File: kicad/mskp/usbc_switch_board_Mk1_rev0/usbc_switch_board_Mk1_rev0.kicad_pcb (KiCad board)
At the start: 2 copper layers, 23 parts, among them J1 USB_C_Receptacle_USB2.0_14P, J2 USB_C_Receptacle_USB2.0_14P, J3 USB_A, J4 USB_out_pads, J5 switch_ctrl_pads, Q1 2N3906, Q2 2N3904, U1 FSUSB42MUX, U2 AMS1117-3.3

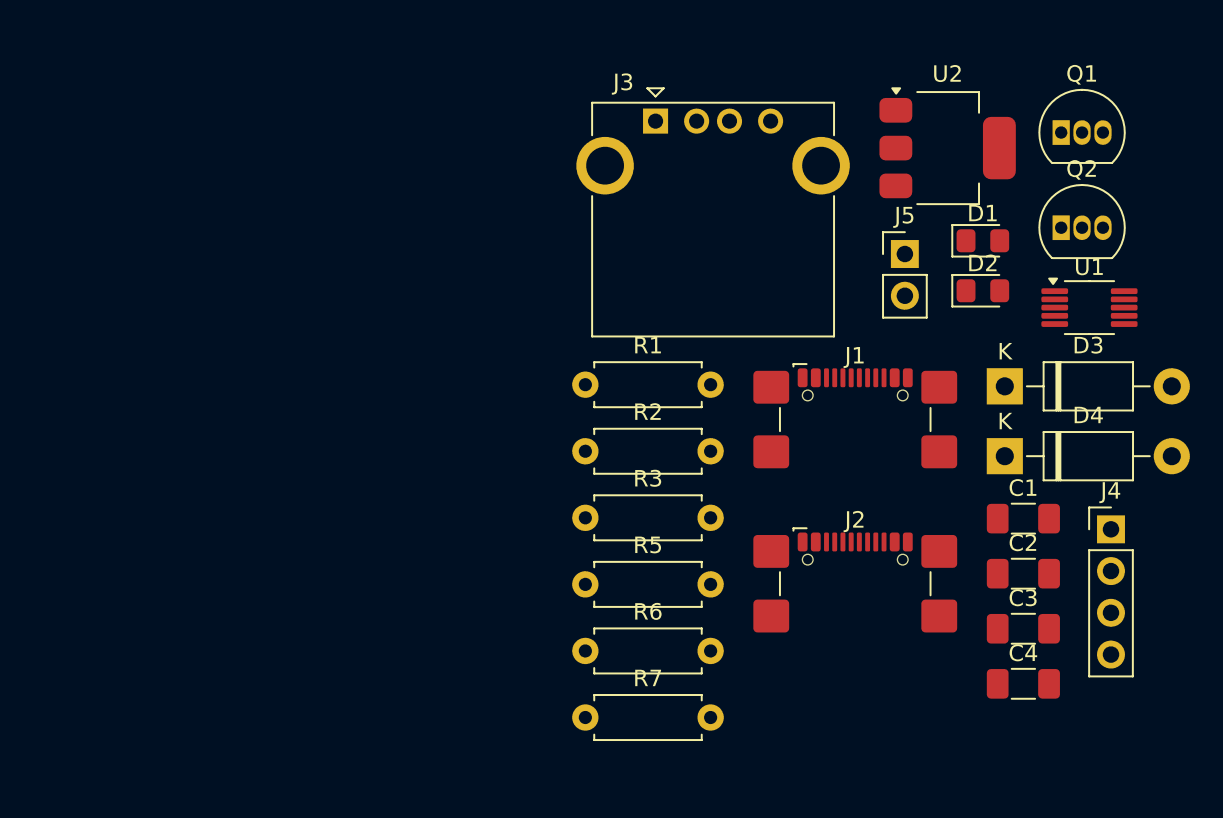
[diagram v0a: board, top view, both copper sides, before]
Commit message: Begins rough PCB part grouping for all control board revisions
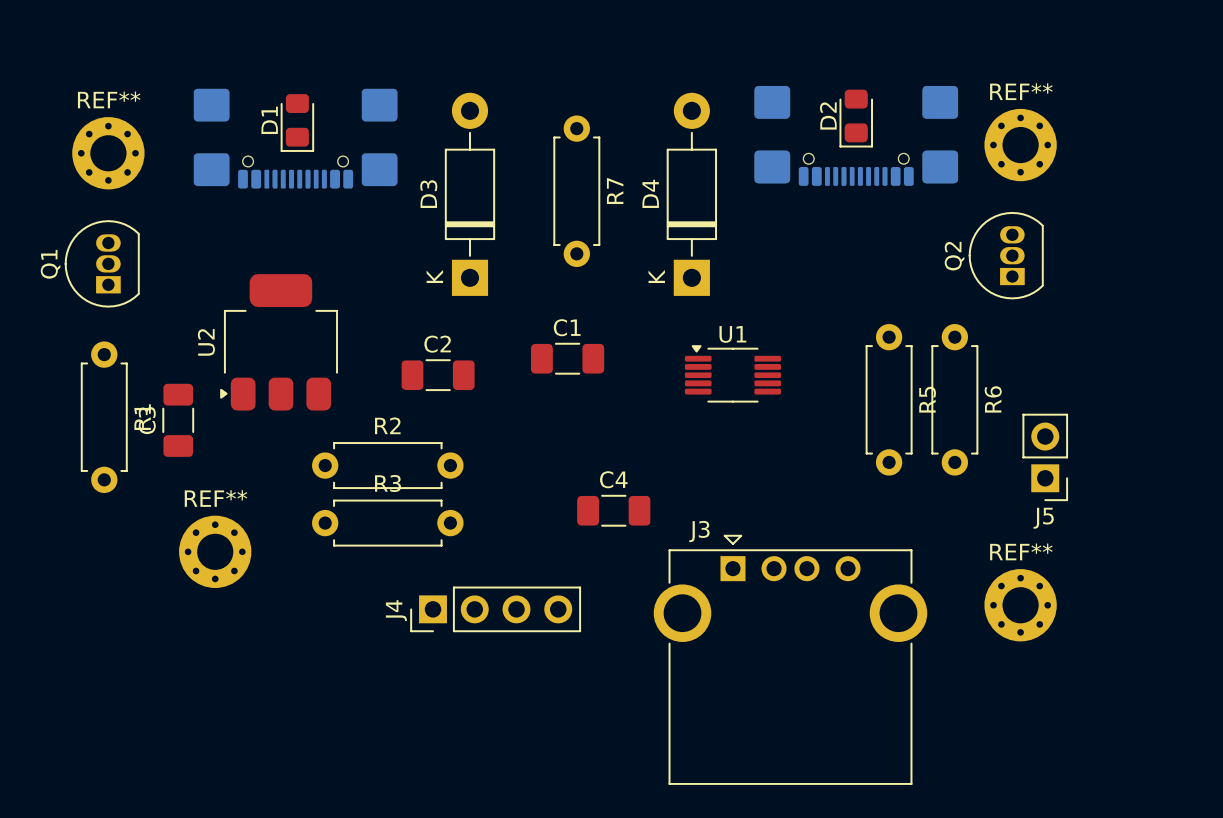
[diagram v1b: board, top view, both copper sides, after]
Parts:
- added REF**: MountingHole_2.2mm_M2_Pad_Via, MountingHole:MountingHole_2.2mm_M2_Pad_Via, F.Cu at (159.5, 97.0)
- added REF**: MountingHole_2.2mm_M2_Pad_Via, MountingHole:MountingHole_2.2mm_M2_Pad_Via, F.Cu at (159.5, 69.0)
- added REF**: MountingHole_2.2mm_M2_Pad_Via, MountingHole:MountingHole_2.2mm_M2_Pad_Via, F.Cu at (104.0, 69.5)
- added REF**: MountingHole_2.2mm_M2_Pad_Via, MountingHole:MountingHole_2.2mm_M2_Pad_Via, F.Cu at (110.5, 93.8)
- J1, J2: moved to B.Cu
- moved Q1 58.7 mm to (104.0, 77.5), turned to 90 degrees
- moved C3 53.0 mm to (108.2, 85.8), turned to 90 degrees
- moved D1 42.3 mm to (115.5, 67.5), turned to 90 degrees
- moved U2 42.2 mm to (114.5, 81.0), turned to 90 degrees
- moved J4 41.5 mm to (123.8, 97.2), turned to 90 degrees
- moved J1 39.2 mm to (115.4, 67.4)
- moved C2 37.6 mm to (124.1, 83.0)
- moved R7 35.8 mm to (132.5, 68.0), turned to -90 degrees
- moved D3 33.2 mm to (126.0, 77.1), turned to 90 degrees
- moved J2 29.6 mm to (149.5, 67.2)
- moved R6 29.5 mm to (155.5, 80.7), turned to -90 degrees
- moved C1 29.4 mm to (131.9, 82.0)
- moved R1 29.3 mm to (103.8, 81.8), turned to -90 degrees
- moved J3 27.6 mm to (142.0, 94.8)
- moved C4 27.1 mm to (134.8, 91.2)
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
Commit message: Continues work with rough PCB outlines
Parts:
- moved C3 14.3 mm to (122.5, 84.9), turned to 180 degrees
- moved J3 7.97 mm to (138.2, 87.7)
- moved R6 7.48 mm to (148.1, 79.8), turned to 0 degrees
- moved REF** 7.16 mm to (154.4, 91.9)
- moved J5 6.10 mm to (155.2, 87.4), turned to -90 degrees
- moved C4 5.94 mm to (129.5, 88.4)
- moved R2 5.94 mm to (111.3, 88.5)
- moved R3 5.94 mm to (111.3, 92.0)
- moved Q2 5.89 mm to (153.2, 76.3)
- moved REF** 5.07 mm to (154.4, 69.2)
- moved J2 4.94 mm to (144.8, 68.6)
- moved D2 4.87 mm to (144.8, 68.4), turned to 0 degrees
- moved J4 4.86 mm to (122.9, 92.5)
- moved REF** 4.80 mm to (106.0, 91.9)
- moved D4 4.48 mm to (135.2, 78.3)
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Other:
- board outline added: 54.4 x 29 mm

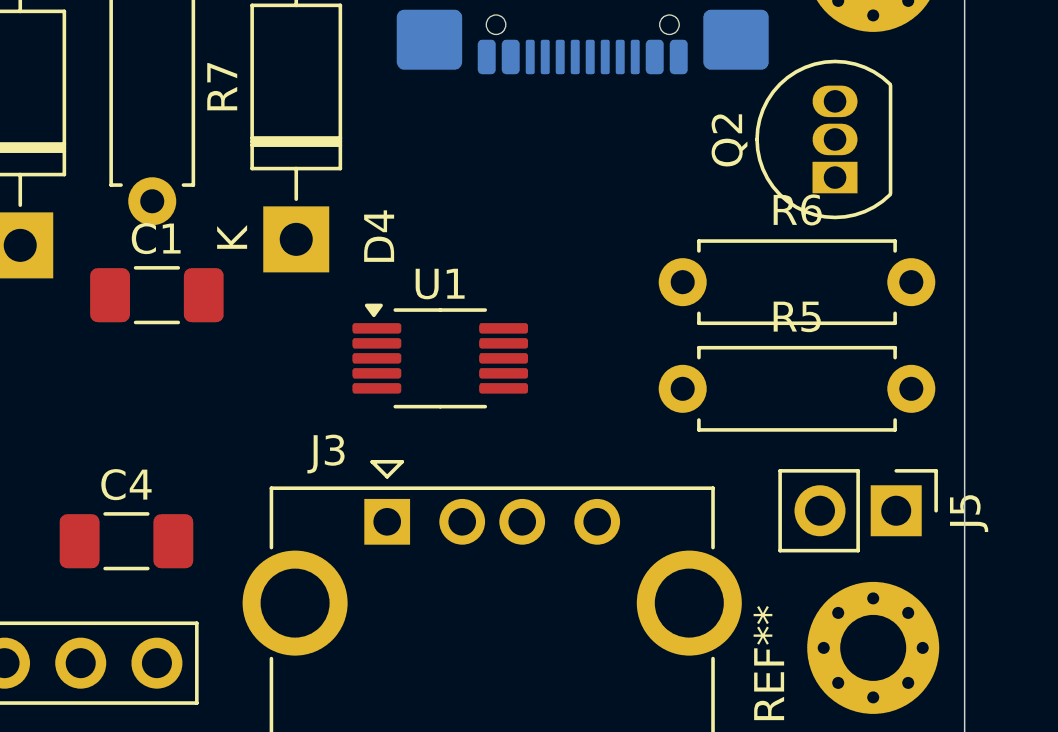
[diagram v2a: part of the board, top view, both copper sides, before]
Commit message: Refining PCB outlines for pico and io control boards
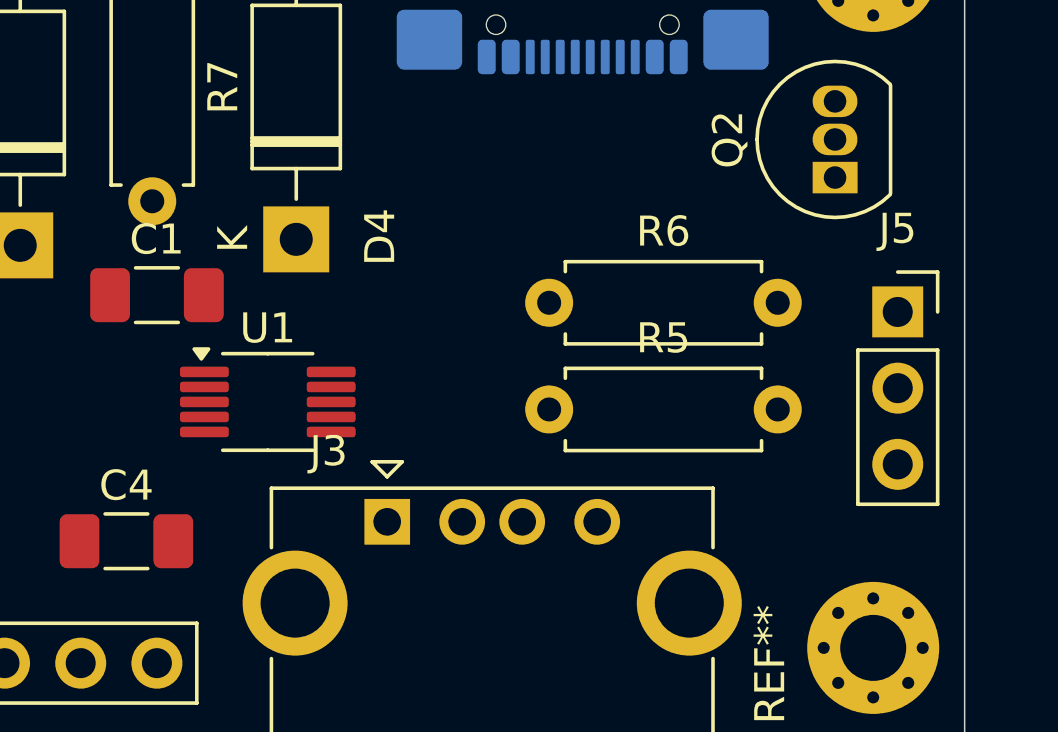
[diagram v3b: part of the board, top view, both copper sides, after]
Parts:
- J5: value switch_ctrl_pads -> Switch_ctrl_pads; footprint Connector_PinHeader_2.54mm:PinHeader_1x02_P2.54mm_Vertical -> Connector_PinSocket_2.54mm:PinSocket_1x03_P2.54mm_Vertical
- moved J5 6.63 mm to (155.2, 80.8), turned to 0 degrees
- moved U1 5.93 mm to (134.2, 83.8)
- moved R5 4.50 mm to (143.6, 84.0)
- moved R6 4.50 mm to (143.6, 80.4)
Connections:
- J5 pad 1: /SEL -> GND
- J5 pad 2: /SUS -> /SEL
- R6 pad 2: /SUS -> Net-(J5-Pin_3)
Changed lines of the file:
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@@
 	(net 16 "/D-")
 	(net 17 "/D+")
-	(net 18 "/SUS")
-	(net 19 "/SEL")
-	(net 20 "Net-(Q1-E)")
-	(net 21 "Net-(Q1-B)")
-	(net 22 "Net-(U2-GND)")
-	(net 23 "Net-(U1-SEL)")
-	(net 24 "Net-(U1-~{OE})")
+	(net 18 "/SEL")
+	(net 19 "Net-(Q1-E)")
+	(net 20 "Net-(Q1-B)")
+	(net 21 "Net-(U2-GND)")
+	(net 22 "Net-(U1-SEL)")
+	(net 23 "Net-(U1-~{OE})")
+	(net 24 "Net-(J5-Pin_3)")
 	(footprint "MountingHole:MountingHole_2.2mm_M2_Pad_Via"
 		(layer "F.Cu")
@@
 	(footprint "Package_SO:MSOP-10_3x3mm_P0.5mm"
 		(layer "F.Cu")
-		(at 140 82.296)
+		(at 134.25 83.75)
 		(descr "MSOP, 10 Pin (https://www.jedec.org/system/files/docs/mo-187F.pdf variant BA), generated with kicad-footprint-generator ipc_gullwing_generator.py")
 		(tags "MSOP SO")
@@
 			(layers "F.Cu" "F.Paste" "F.Mask")
 			(roundrect_rratio 0.25)
-			(net 23 "Net-(U1-SEL)")
+			(net 22 "Net-(U1-SEL)")
 			(pinfunction "SEL")
 			(pintype "input")
@@
 			(layers "F.Cu" "F.Paste" "F.Mask")
 			(roundrect_rratio 0.25)
-			(net 24 "Net-(U1-~{OE})")
+			(net 23 "Net-(U1-~{OE})")
 			(pinfunction "~{OE}")
 			(pintype "input")
@@
 			(layers "*.Cu" "*.Mask")
 			(remove_unused_layers no)
-			(net 20 "Net-(Q1-E)")
+			(net 19 "Net-(Q1-E)")
 			(pinfunction "E")
 			(pintype "passive")
@@
 			(layers "*.Cu" "*.Mask")
 			(remove_unused_layers no)
-			(net 21 "Net-(Q1-B)")
+			(net 20 "Net-(Q1-B)")
 			(pinfunction "B")
 			(pintype "input")
@@
 			(layers "*.Cu" "*.Mask")
 			(remove_unused_layers no)
-			(net 22 "Net-(U2-GND)")
+			(net 21 "Net-(U2-GND)")
 			(pintype "passive")
 		)
@@
 		(tags "LED handsolder")
 		(property "Reference" "D2"
-			(at 0 -1.65 360)
+			(at 0 -1.65 0)
 			(layer "F.SilkS")
 			(effects
@@
 		)
 		(property "Value" "LED"
-			(at 0 1.65 360)
+			(at 0 1.65 0)
 			(layer "F.Fab")
 			(effects
@@
 		)
 		(fp_text user "${REFERENCE}"
-			(at 0 0 360)
+			(at 0 0 0)
 			(layer "F.Fab")
 			(effects
@@
 	(footprint "Resistor_THT:R_Axial_DIN0207_L6.3mm_D2.5mm_P7.62mm_Horizontal"
 		(layer "F.Cu")
-		(at 148.082 79.756)
+		(at 143.63 80.444)
 		(descr "Resistor, Axial_DIN0207 series, Axial, Horizontal, pin pitch=7.62mm, 0.25W = 1/4W, length*diameter=6.3*2.5mm^2, http://cdn-reichelt.de/documents/datenblatt/B400/1_4W%23YAG.pdf")
 		(tags "Resistor Axial_DIN0207 series Axial Horizontal pin pitch 7.62mm 0.25W = 1/4W length 6.3mm diameter 2.5mm")
 		(property "Reference" "R6"
-			(at 3.81 -2.37 360)
+			(at 3.81 -2.37 0)
 			(layer "F.SilkS")
 			(effects
@@
 		)
 		(property "Value" "10K"
-			(at 3.81 2.37 360)
+			(at 3.81 2.37 0)
 			(layer "F.Fab")
 			(effects
@@
 		)
 		(fp_text user "${REFERENCE}"
-			(at 3.81 0 360)
+			(at 3.81 0 0)
 			(layer "F.Fab")
 			(effects
@@
 			(layers "*.Cu" "*.Mask")
 			(remove_unused_layers no)
-			(net 24 "Net-(U1-~{OE})")
+			(net 23 "Net-(U1-~{OE})")
 			(pintype "passive")
 		)
@@
 			(layers "*.Cu" "*.Mask")
 			(remove_unused_layers no)
-			(net 18 "/SUS")
+			(net 24 "Net-(J5-Pin_3)")
 			(pintype "passive")
 		)
@@
 			(layers "*.Cu" "*.Mask")
 			(remove_unused_layers no)
-			(net 21 "Net-(Q1-B)")
+			(net 20 "Net-(Q1-B)")
 			(pinfunction "B")
 			(pintype "passive")
@@
 			(layers "*.Cu" "*.Mask")
 			(remove_unused_layers no)
-			(net 20 "Net-(Q1-E)")
+			(net 19 "Net-(Q1-E)")
 			(pinfunction "C")
 			(pintype "passive")
@@
 			(layers "*.Cu" "*.Mask")
 			(remove_unused_layers no)
-			(net 20 "Net-(Q1-E)")
+			(net 19 "Net-(Q1-E)")
 			(pintype "passive")
 		)
@@
 			(layers "*.Cu" "*.Mask")
 			(remove_unused_layers no)
-			(net 21 "Net-(Q1-B)")
+			(net 20 "Net-(Q1-B)")
 			(pintype "passive")
 		)
@@
 			(layers "*.Cu" "*.Mask")
 			(remove_unused_layers no)
-			(net 19 "/SEL")
+			(net 18 "/SEL")
 			(pintype "passive")
 		)
@@
 		(tags "LED handsolder")
 		(property "Reference" "D1"
-			(at 0 -1.65 360)
+			(at 0 -1.65 0)
 			(layer "F.SilkS")
 			(effects
@@
 		)
 		(property "Value" "LED"
-			(at 0 1.65 360)
+			(at 0 1.65 0)
 			(layer "F.Fab")
 			(effects
@@
 		)
 		(fp_text user "${REFERENCE}"
-			(at 0 0 360)
+			(at 0 0 0)
 			(layer "F.Fab")
 			(effects
@@
 			(layers "*.Cu" "*.Mask")
 			(remove_unused_layers no)
-			(net 22 "Net-(U2-GND)")
+			(net 21 "Net-(U2-GND)")
 			(pintype "passive")
 		)
@@
 	(footprint "Resistor_THT:R_Axial_DIN0207_L6.3mm_D2.5mm_P7.62mm_Horizontal"
 		(layer "F.Cu")
-		(at 148.082 83.312)
+		(at 143.63 84)
 		(descr "Resistor, Axial_DIN0207 series, Axial, Horizontal, pin pitch=7.62mm, 0.25W = 1/4W, length*diameter=6.3*2.5mm^2, http://cdn-reichelt.de/documents/datenblatt/B400/1_4W%23YAG.pdf")
 		(tags "Resistor Axial_DIN0207 series Axial Horizontal pin pitch 7.62mm 0.25W = 1/4W length 6.3mm diameter 2.5mm")
 		(property "Reference" "R5"
-			(at 3.81 -2.37 360)
+			(at 3.81 -2.37 0)
 			(layer "F.SilkS")
 			(effects
@@
 		)
 		(property "Value" "10K"
-			(at 3.81 2.37 360)
+			(at 3.81 2.37 0)
 			(layer "F.Fab")
 			(effects
@@
 		)
 		(fp_text user "${REFERENCE}"
-			(at 3.81 0 360)
+			(at 3.81 0 0)
 			(layer "F.Fab")
 			(effects
@@
 			(layers "*.Cu" "*.Mask")
 			(remove_unused_layers no)
-			(net 23 "Net-(U1-SEL)")
+			(net 22 "Net-(U1-SEL)")
 			(pintype "passive")
 		)
@@
 			(layers "*.Cu" "*.Mask")
 			(remove_unused_layers no)
-			(net 19 "/SEL")
+			(net 18 "/SEL")
 			(pintype "passive")
 		)
@@
 		)
 	)
-	(footprint "Connector_PinHeader_2.54mm:PinHeader_1x02_P2.54mm_Vertical"
+	(footprint "Connector_PinSocket_2.54mm:PinSocket_1x03_P2.54mm_Vertical"
 		(layer "F.Cu")
-		(at 155.199 87.376 -90)
-		(descr "Through hole straight pin header, 1x02, 2.54mm pitch, single row")
-		(tags "Through hole pin header THT 1x02 2.54mm single row")
+		(at 155.25 80.75)
+		(descr "Through hole straight socket strip, 1x03, 2.54mm pitch, single row (from Kicad 4.0.7), script generated")
+		(tags "Through hole socket strip THT 1x03 2.54mm single row")
 		(property "Reference" "J5"
-			(at 0 -2.33 90)
+			(at 0 -2.77 0)
 			(layer "F.SilkS")
 			(effects
@@
 			)
 		)
-		(property "Value" "switch_ctrl_pads"
-			(at 0 4.87 90)
+		(property "Value" "Switch_ctrl_pads"
+			(at 0 7.85 0)
 			(layer "F.Fab")
 			(effects
@@
 			)
 		)
-		(property "Footprint" "Connector_PinHeader_2.54mm:PinHeader_1x02_P2.54mm_Vertical"
-			(at 0 0 -90)
+		(property "Footprint" "Connector_PinSocket_2.54mm:PinSocket_1x03_P2.54mm_Vertical"
+			(at 0 0 0)
 			(unlocked yes)
 			(layer "F.Fab")
@@
 		)
 		(property "Datasheet" ""
-			(at 0 0 -90)
+			(at 0 0 0)
 			(unlocked yes)
 			(layer "F.Fab")
@@
 			)
 		)
-		(property "Description" "Generic connector, single row, 01x02, script generated"
-			(at 0 0 -90)
+		(property "Description" "Generic connector, single row, 01x03, script generated"
+			(at 0 0 0)
 			(unlocked yes)
 			(layer "F.Fab")
@@
 		(attr through_hole)
 		(fp_line
-			(start -1.33 3.87)
-			(end 1.33 3.87)
+			(start -1.33 1.27)
+			(end -1.33 6.41)
 			(stroke
 				(width 0.12)
@@
 		(fp_line
 			(start -1.33 1.27)
-			(end -1.33 3.87)
+			(end 1.33 1.27)
 			(stroke
 				(width 0.12)
@@
 		)
 		(fp_line
-			(start -1.33 1.27)
-			(end 1.33 1.27)
+			(start -1.33 6.41)
+			(end 1.33 6.41)
 			(stroke
 				(width 0.12)
@@
 		)
 		(fp_line
-			(start 1.33 1.27)
-			(end 1.33 3.87)
+			(start 0 -1.33)
+			(end 1.33 -1.33)
 			(stroke
 				(width 0.12)
@@
 		)
 		(fp_line
-			(start -1.33 0)
-			(end -1.33 -1.33)
+			(start 1.33 -1.33)
+			(end 1.33 0)
 			(stroke
 				(width 0.12)
@@
 		)
 		(fp_line
-			(start -1.33 -1.33)
-			(end 0 -1.33)
+			(start 1.33 1.27)
+			(end 1.33 6.41)
 			(stroke
 				(width 0.12)
@@
 		)
 		(fp_line
-			(start -1.8 4.35)
-			(end 1.8 4.35)
+			(start -1.8 -1.8)
+			(end 1.75 -1.8)
 			(stroke
 				(width 0.05)
@@
 		)
 		(fp_line
-			(start 1.8 4.35)
-			(end 1.8 -1.8)
+			(start -1.8 6.85)
+			(end -1.8 -1.8)
 			(stroke
 				(width 0.05)
@@
 		)
 		(fp_line
-			(start -1.8 -1.8)
-			(end -1.8 4.35)
+			(start 1.75 -1.8)
+			(end 1.75 6.85)
 			(stroke
 				(width 0.05)
@@
 		)
 		(fp_line
-			(start 1.8 -1.8)
-			(end -1.8 -1.8)
+			(start 1.75 6.85)
+			(end -1.8 6.85)
 			(stroke
 				(width 0.05)
@@
 		)
 		(fp_line
-			(start -1.27 3.81)
-			(end -1.27 -0.635)
+			(start -1.27 -1.27)
+			(end 0.635 -1.27)
 			(stroke
 				(width 0.1)
@@
 		)
 		(fp_line
-			(start 1.27 3.81)
-			(end -1.27 3.81)
+			(start -1.27 6.35)
+			(end -1.27 -1.27)
 			(stroke
 				(width 0.1)
@@
 		)
 		(fp_line
-			(start -1.27 -0.635)
-			(end -0.635 -1.27)
+			(start 0.635 -1.27)
+			(end 1.27 -0.635)
 			(stroke
 				(width 0.1)
@@
 		)
 		(fp_line
-			(start -0.635 -1.27)
-			(end 1.27 -1.27)
+			(start 1.27 -0.635)
+			(end 1.27 6.35)
 			(stroke
 				(width 0.1)
@@
 		)
 		(fp_line
-			(start 1.27 -1.27)
-			(end 1.27 3.81)
+			(start 1.27 6.35)
+			(end -1.27 6.35)
 			(stroke
 				(width 0.1)
@@
 		)
 		(fp_text user "${REFERENCE}"
-			(at 0 1.27 180)
+			(at 0 2.54 90)
 			(layer "F.Fab")
 			(effects
@@
 		)
 		(pad "1" thru_hole rect
-			(at 0 0 270)
+			(at 0 0)
 			(size 1.7 1.7)
 			(drill 1)
 			(layers "*.Cu" "*.Mask")
 			(remove_unused_layers no)
-			(net 19 "/SEL")
+			(net 1 "GND")
 			(pinfunction "Pin_1")
 			(pintype "passive")
 		)
 		(pad "2" thru_hole oval
-			(at 0 2.54 270)
+			(at 0 2.54)
 			(size 1.7 1.7)
 			(drill 1)
 			(layers "*.Cu" "*.Mask")
 			(remove_unused_layers no)
-			(net 18 "/SUS")
+			(net 18 "/SEL")
 			(pinfunction "Pin_2")
 			(pintype "passive")
 		)
-		(model "${KICAD8_3DMODEL_DIR}/Connector_PinHeader_2.54mm.3dshapes/PinHeader_1x02_P2.54mm_Vertical.wrl"
+		(pad "3" thru_hole oval
+			(at 0 5.08)
+			(size 1.7 1.7)
+			(drill 1)
+			(layers "*.Cu" "*.Mask")
+			(remove_unused_layers no)
+			(net 24 "Net-(J5-Pin_3)")
+			(pinfunction "Pin_3")
+			(pintype "passive")
+		)
+		(model "${KICAD8_3DMODEL_DIR}/Connector_PinSocket_2.54mm.3dshapes/PinSocket_1x03_P2.54mm_Vertical.wrl"
 			(offset
 				(xyz 0 0 0)
@@
 			(layers "F.Cu" "F.Paste" "F.Mask")
 			(roundrect_rratio 0.25)
-			(net 22 "Net-(U2-GND)")
+			(net 21 "Net-(U2-GND)")
 			(pinfunction "GND")
 			(pintype "power_in")
